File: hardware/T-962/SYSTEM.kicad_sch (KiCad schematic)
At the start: 6 parts

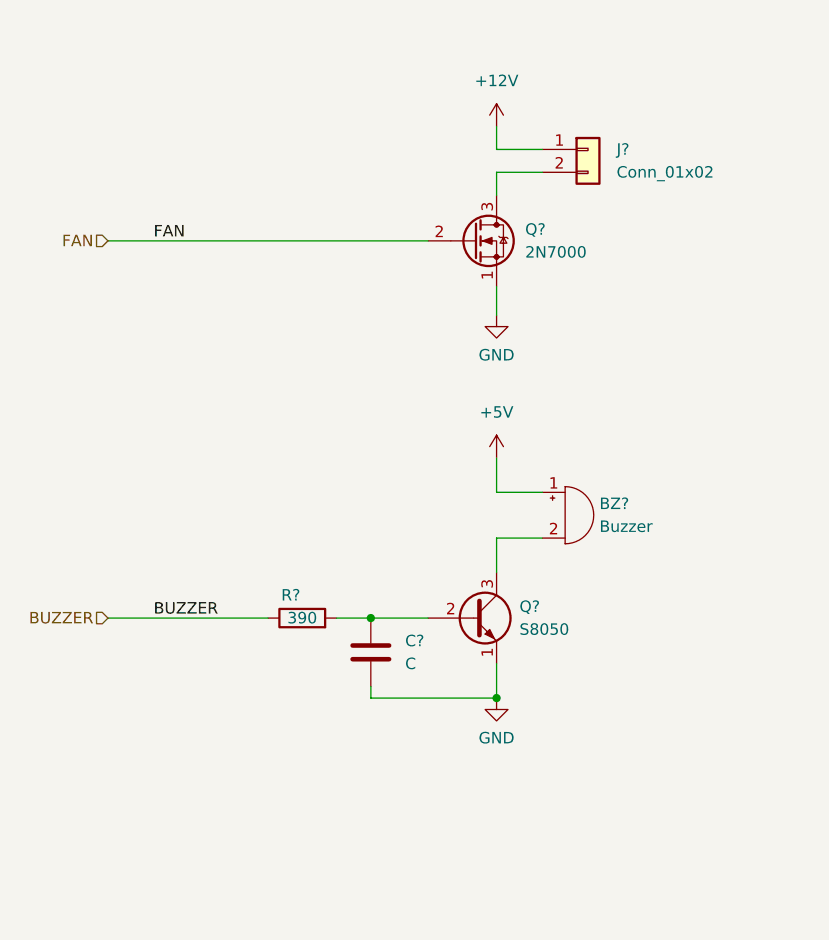
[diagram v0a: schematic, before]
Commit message: fill out designators
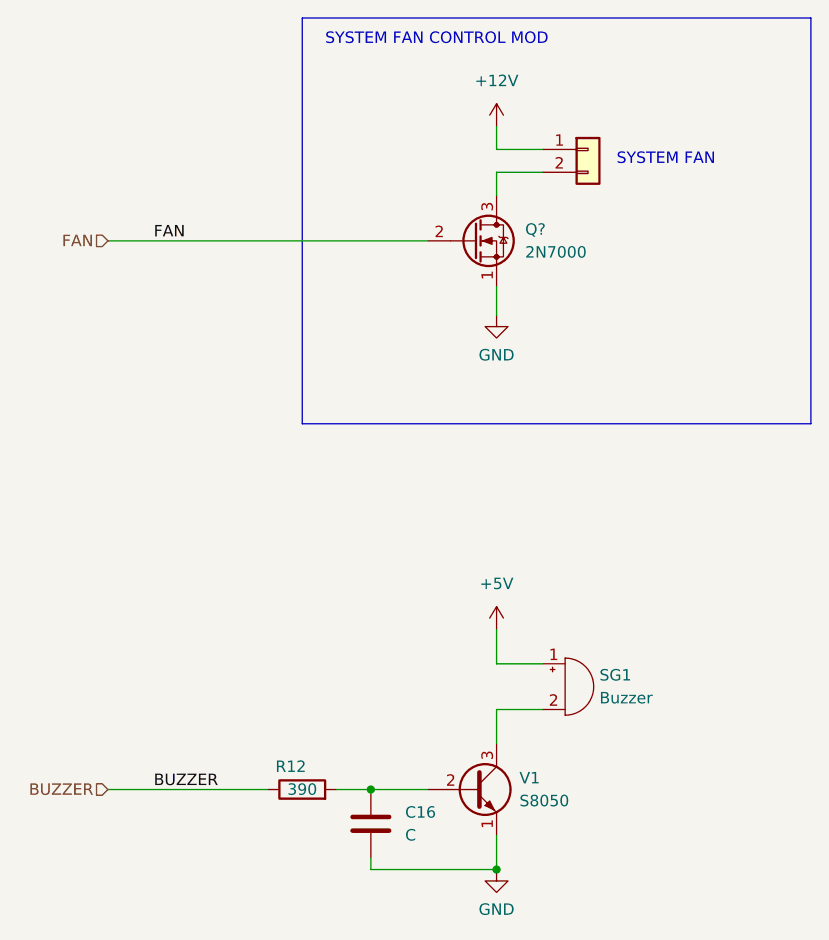
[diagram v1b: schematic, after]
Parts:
- gave numbers to parts that had none: 4
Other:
- note added: "SYSTEM FAN"
- note added: "SYSTEM FAN CONTROL MOD"
- moved on the sheet: C16, R12, SG1, V1
